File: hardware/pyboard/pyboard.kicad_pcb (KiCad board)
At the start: 2 copper layers, 65 parts, among them J1 Battery, J2 Arduino_Mega2560_Shield, J6 USB_B_Micro, J9 Micro_SD_SCHA5B0200, Q1 IRLML6402, Q2 IRLML6402, SW1 RST, SW2 USR, U1 STM32F405RGT6, U2 MCP1703A-3302_SOT89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

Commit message: Swap Y and X pins
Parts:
- D1, D3, D4, D5, D6: footprint LED_SMD:LED_1206_3216Metric -> LED_SMD:LED_0603_1608Metric
- moved Q1 76.5 mm to (116.0, 112.0)
- moved D4 72.0 mm to (103.5, 96.0)
- moved D6 71.8 mm to (103.5, 100.0)
- moved SW2 65.9 mm to (76.0, 66.0)
- moved SW1 61.2 mm to (65.0, 77.0)
- moved D1 60.9 mm to (103.5, 102.0)
- moved D5 58.8 mm to (103.5, 98.0)
- moved D3 46.4 mm to (103.5, 93.8)
- moved U3 37.1 mm to (116.0, 104.0)
- moved Q2 19.7 mm to (121.7, 104.5)
- moved J1 15.0 mm to (68.0, 97.0)
- moved U1 3.32 mm to (153.0, 92.0)
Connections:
- J2 pad D0: /X4 -> /Y2
- J2 pad D1: /X3 -> /Y1
- J2 pad D16: /Y1 -> /X3
- J2 pad D17: /Y2 -> /X4

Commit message: Remove ISP pin header
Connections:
- J2 pad A10: /Y12 -> /X21
- J2 pad A11: Net-(J2-PadA11) -> /X22
- J2 pad A12: Net-(J2-PadA12) -> /Y11
- J2 pad A13: Net-(J2-PadA13) -> /Y12
- J2 pad A14: Net-(J2-PadA14) -> (no net)
- J2 pad A15: Net-(J2-PadA15) -> (no net)
- J2 pad A3: /X11 -> /X6
- J2 pad A4: /X12 -> /X7
- J2 pad A5: /X19 -> /X8
- J2 pad A6: /X20 -> /X11
- J2 pad A7: /X21 -> /X12
- J2 pad A8: /X22 -> /X19
- J2 pad A9: /Y11 -> /X20
- J2 pad AREF: Net-(J2-PadAREF) -> (no net)
- J2 pad D10: /SW -> /GRN
- J2 pad D13: /GRN -> /SW
- J2 pad D14: Net-(J2-PadD14) -> /X3
- J2 pad D15: Net-(J2-PadD15) -> /X4
- J2 pad D16: /X3 -> (no net)
- J2 pad D17: /X4 -> (no net)
- J2 pad D18: Net-(J2-PadD18) -> (no net)
- J2 pad D19: Net-(J2-PadD19) -> (no net)
- J2 pad D22: /RED -> /BOOT0
- J2 pad D23: Net-(J2-PadD23) -> (no net)
- J2 pad D24: Net-(J2-PadD24) -> (no net)
- J2 pad D25: Net-(J2-PadD25) -> (no net)
- J2 pad D26: Net-(J2-PadD26) -> (no net)
- J2 pad D27: Net-(J2-PadD27) -> (no net)
- J2 pad D28: Net-(J2-PadD28) -> (no net)
- J2 pad D29: Net-(J2-PadD29) -> (no net)
- J2 pad D30: Net-(J2-PadD30) -> (no net)
- J2 pad D31: Net-(J2-PadD31) -> (no net)
- J2 pad D32: Net-(J2-PadD32) -> (no net)
- J2 pad D33: Net-(J2-PadD33) -> (no net)
- J2 pad D34: Net-(J2-PadD34) -> (no net)
- J2 pad D35: Net-(J2-PadD35) -> (no net)
- J2 pad D36: Net-(J2-PadD36) -> (no net)
- J2 pad D37: Net-(J2-PadD37) -> (no net)
- J2 pad D38: Net-(J2-PadD38) -> (no net)
- J2 pad D39: Net-(J2-PadD39) -> (no net)
- J2 pad D40: Net-(J2-PadD40) -> (no net)
- J2 pad D41: Net-(J2-PadD41) -> (no net)
- J2 pad D42: Net-(J2-PadD42) -> (no net)
- J2 pad D43: Net-(J2-PadD43) -> (no net)
- J2 pad D44: Net-(J2-PadD44) -> (no net)
- J2 pad D45: Net-(J2-PadD45) -> (no net)
- J2 pad D46: Net-(J2-PadD46) -> (no net)
- J2 pad D47: Net-(J2-PadD47) -> (no net)
- J2 pad D48: Net-(J2-PadD48) -> (no net)
- J2 pad D49: Net-(J2-PadD49) -> (no net)
- J2 pad D50: Net-(J2-PadD50) -> (no net)
- J2 pad D51: Net-(J2-PadD51) -> (no net)
- J2 pad D52: Net-(J2-PadD52) -> (no net)
- J2 pad D53: Net-(J2-PadD53) -> (no net)
- J2 pad D9: /BOOT0 -> /RED
- J2 pad IORF: Net-(J2-PadIORF) -> (no net)
- J6 pad D+: /DP_USB -> (no net)
- J6 pad D-: /DM_USB -> (no net)
- J6 pad GND: GND -> (no net)
- J6 pad ID: /ID_USB -> (no net)
- J6 pad VBUS: /VBUS_USB -> (no net)
- R16 pad 1: /DP_USB -> (no net)
- R17 pad 1: /DM_USB -> (no net)
- R18 pad 1: /ID_USB -> (no net)

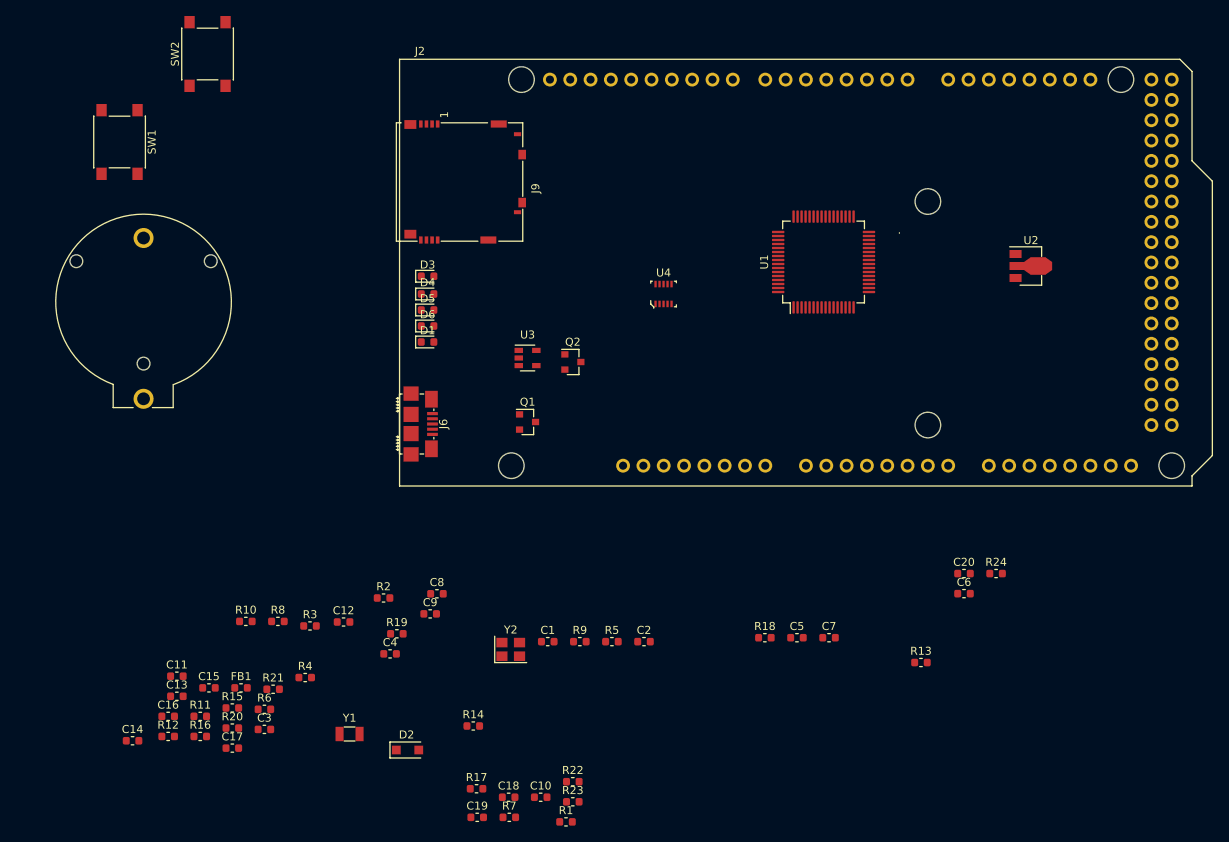
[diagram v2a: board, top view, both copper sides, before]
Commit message: Place power switch and MOSFETs
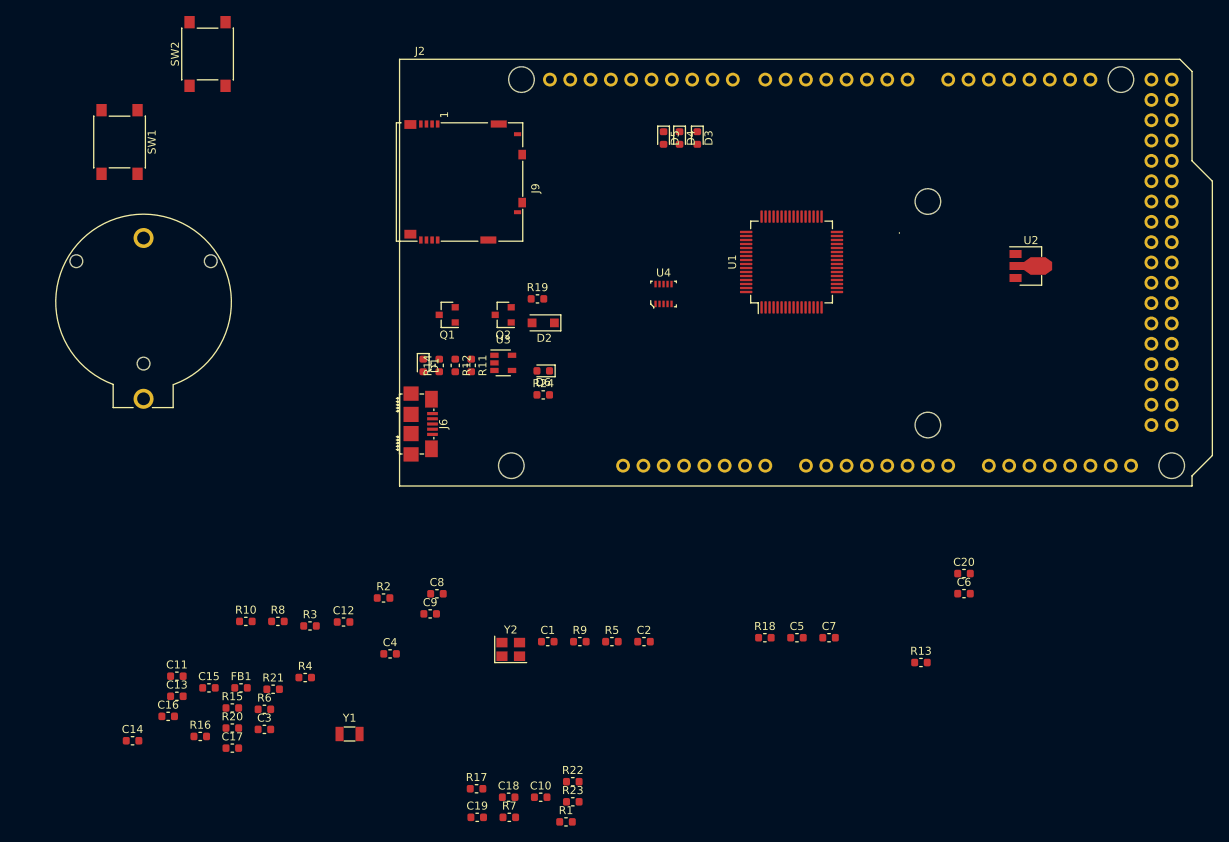
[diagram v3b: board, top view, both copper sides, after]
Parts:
- moved R24 60.9 mm to (118.0, 108.6)
- moved R12 58.6 mm to (107.0, 104.9), turned to 270 degrees
- moved D2 56.0 mm to (118.0, 99.6), turned to 180 degrees
- moved R11 55.4 mm to (109.0, 104.9), turned to 270 degrees
- moved R19 45.4 mm to (117.2, 96.6)
- moved R14 45.3 mm to (105.0, 104.9), turned to 90 degrees
- moved D3 37.9 mm to (137.2, 76.5), turned to 270 degrees
- moved D4 37.0 mm to (135.0, 76.5), turned to 270 degrees
- moved D5 36.5 mm to (133.0, 76.5), turned to 270 degrees
- moved Q1 16.7 mm to (106.0, 98.6), turned to 180 degrees
- moved D6 15.5 mm to (118.0, 105.6), turned to 180 degrees
- moved Q2 10.5 mm to (113.0, 98.6), turned to 180 degrees
- moved U1 4.00 mm to (149.0, 92.0)
- moved U3 3.10 mm to (113.0, 104.6)
- moved D1 2.98 mm to (103.0, 104.9), turned to 270 degrees
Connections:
- J2 pad A14: (no net) -> Net-(J2-PadA14)
- J2 pad A15: (no net) -> Net-(J2-PadA15)
- J2 pad AREF: (no net) -> Net-(J2-PadAREF)
- J2 pad D16: (no net) -> Net-(J2-PadD16)
- J2 pad D17: (no net) -> Net-(J2-PadD17)
- J2 pad D18: (no net) -> Net-(J2-PadD18)
- J2 pad D19: (no net) -> Net-(J2-PadD19)
- J2 pad D23: (no net) -> Net-(J2-PadD23)
- J2 pad D24: (no net) -> Net-(J2-PadD24)
- J2 pad D25: (no net) -> Net-(J2-PadD25)
- J2 pad D26: (no net) -> Net-(J2-PadD26)
- J2 pad D27: (no net) -> Net-(J2-PadD27)
- J2 pad D28: (no net) -> Net-(J2-PadD28)
- J2 pad D29: (no net) -> Net-(J2-PadD29)
- J2 pad D30: (no net) -> Net-(J2-PadD30)
- J2 pad D31: (no net) -> Net-(J2-PadD31)
- J2 pad D32: (no net) -> Net-(J2-PadD32)
- J2 pad D33: (no net) -> Net-(J2-PadD33)
- J2 pad D34: (no net) -> Net-(J2-PadD34)
- J2 pad D35: (no net) -> Net-(J2-PadD35)
- J2 pad D36: (no net) -> Net-(J2-PadD36)
- J2 pad D37: (no net) -> Net-(J2-PadD37)
- J2 pad D38: (no net) -> Net-(J2-PadD38)
- J2 pad D39: (no net) -> Net-(J2-PadD39)
- J2 pad D40: (no net) -> Net-(J2-PadD40)
- J2 pad D41: (no net) -> Net-(J2-PadD41)
- J2 pad D42: (no net) -> Net-(J2-PadD42)
- J2 pad D43: (no net) -> Net-(J2-PadD43)
- J2 pad D44: (no net) -> Net-(J2-PadD44)
- J2 pad D45: (no net) -> Net-(J2-PadD45)
- J2 pad D46: (no net) -> Net-(J2-PadD46)
- J2 pad D47: (no net) -> Net-(J2-PadD47)
- J2 pad D48: (no net) -> Net-(J2-PadD48)
- J2 pad D49: (no net) -> Net-(J2-PadD49)
- J2 pad D50: (no net) -> Net-(J2-PadD50)
- J2 pad D51: (no net) -> Net-(J2-PadD51)
- J2 pad D52: (no net) -> Net-(J2-PadD52)
- J2 pad D53: (no net) -> Net-(J2-PadD53)
- J2 pad IORF: (no net) -> Net-(J2-PadIORF)
- J6 pad CGND: (no net) -> GND
- J6 pad D+: (no net) -> /DP_USB
- J6 pad D-: (no net) -> /DM_USB
- J6 pad GND: (no net) -> GND
- J6 pad ID: (no net) -> /ID_USB
- J6 pad VBUS: (no net) -> /VBUS_USB
- R16 pad 1: (no net) -> /DP_USB
- R17 pad 1: (no net) -> /DM_USB
- R18 pad 1: (no net) -> /ID_USB

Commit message: Place voltage regulator
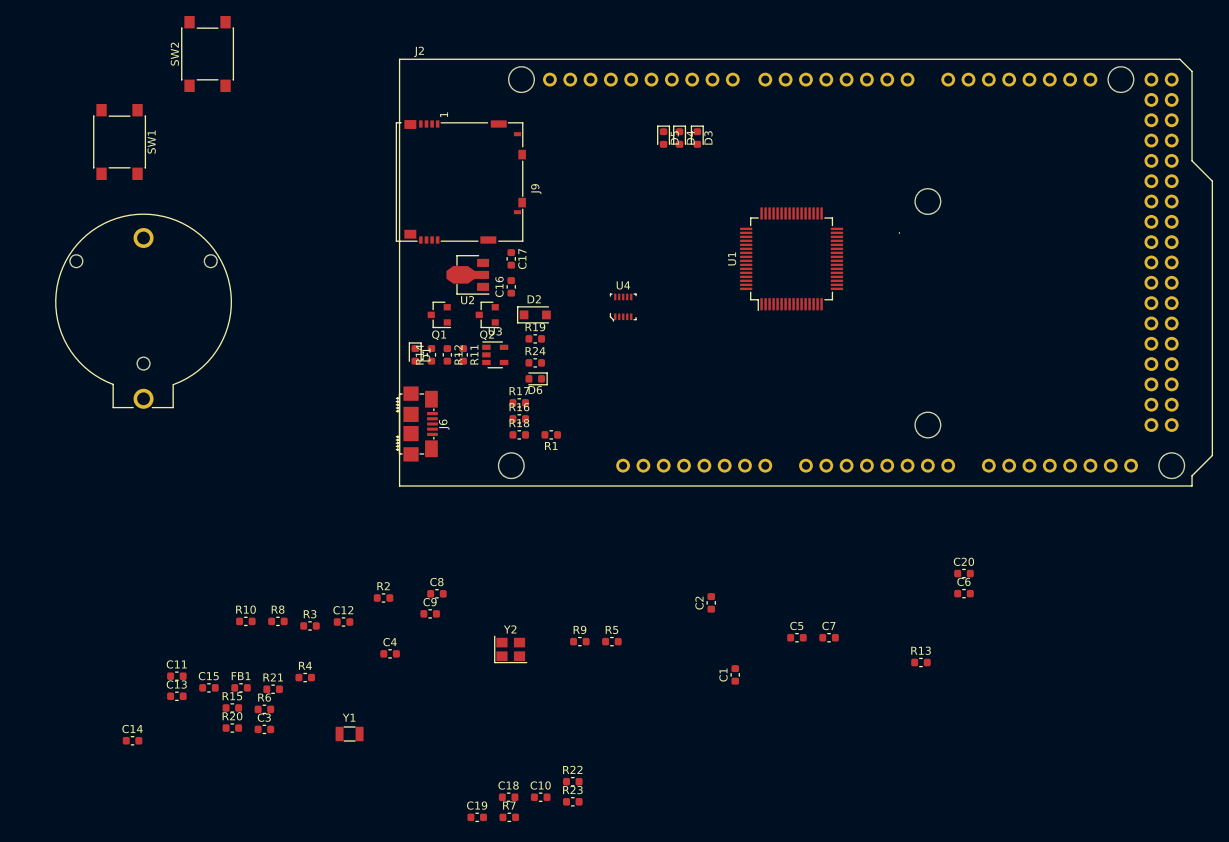
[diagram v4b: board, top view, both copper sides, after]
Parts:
- moved C17 70.4 mm to (114.0, 91.6), turned to 270 degrees
- moved U2 69.5 mm to (109.0, 93.6), turned to 180 degrees
- moved C16 68.7 mm to (114.0, 95.1), turned to 90 degrees
- moved R16 56.3 mm to (115.0, 111.6)
- moved R17 48.5 mm to (115.0, 109.6)
- moved R1 48.4 mm to (119.0, 113.6), turned to 180 degrees
- moved R18 39.8 mm to (115.0, 113.6)
- moved C1 23.8 mm to (142.0, 143.6), turned to 90 degrees
- moved C2 9.70 mm to (139.0, 134.6), turned to 90 degrees
- moved U4 5.29 mm to (128.0, 97.6)
- moved R19 5.01 mm to (117.0, 101.6)
- moved R24 4.12 mm to (117.0, 104.6)
- moved Q2 2.00 mm to (111.0, 98.6)
- moved D1 1.66 mm to (102.0, 103.6)
- moved R11 1.66 mm to (108.0, 103.6)
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
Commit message: Place Y2 crystal oscillator
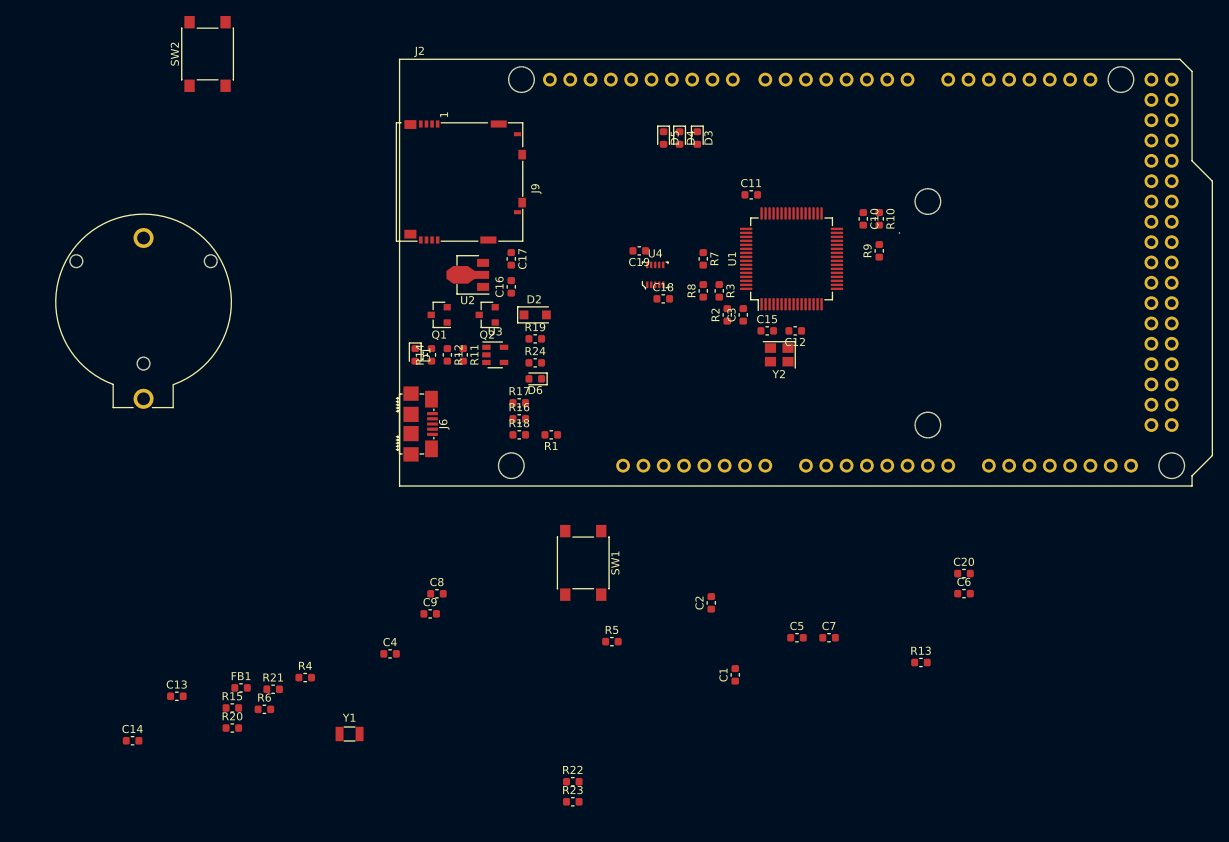
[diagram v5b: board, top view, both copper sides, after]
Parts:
- moved R10 93.8 mm to (160.0, 86.6), turned to 270 degrees
- moved C11 93.7 mm to (144.0, 83.6)
- moved C15 82.8 mm to (146.0, 100.6)
- moved C10 82.8 mm to (158.0, 86.6), turned to 270 degrees
- moved C3 79.2 mm to (143.0, 98.6), turned to 90 degrees
- moved SW1 78.3 mm to (123.0, 129.6)
- moved R7 73.9 mm to (138.0, 91.6), turned to 270 degrees
- moved C19 73.6 mm to (130.0, 90.6), turned to 180 degrees
- moved R8 67.3 mm to (138.0, 95.6), turned to 90 degrees
- moved C12 67.2 mm to (149.5, 100.6), turned to 180 degrees
- moved R3 66.1 mm to (140.0, 95.6), turned to 270 degrees
- moved C18 65.2 mm to (133.0, 96.6)
- moved R9 61.5 mm to (160.0, 90.6), turned to 90 degrees
- moved R2 55.7 mm to (141.0, 98.6), turned to 90 degrees
- moved Y2 49.8 mm to (147.5, 103.6), turned to 180 degrees
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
